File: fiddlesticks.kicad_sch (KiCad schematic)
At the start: 59 parts, among them J1 USB_C_Receptacle_USB2.0_16P, J2 Conn_01x04_Pin, J3 Conn_01x04_Pin, J4 Conn_02x04_Counter_Clockwise, J5 Conn_01x02_Pin, SW1 SW_Push, SW2 SW_Push, U1 STM32F411CEUx, U2 USBLC6-2SC6, U3 MCP1640Bx-xCHY, U4 SPX3819M5-L-3-3, Y1 8MHz 18pF

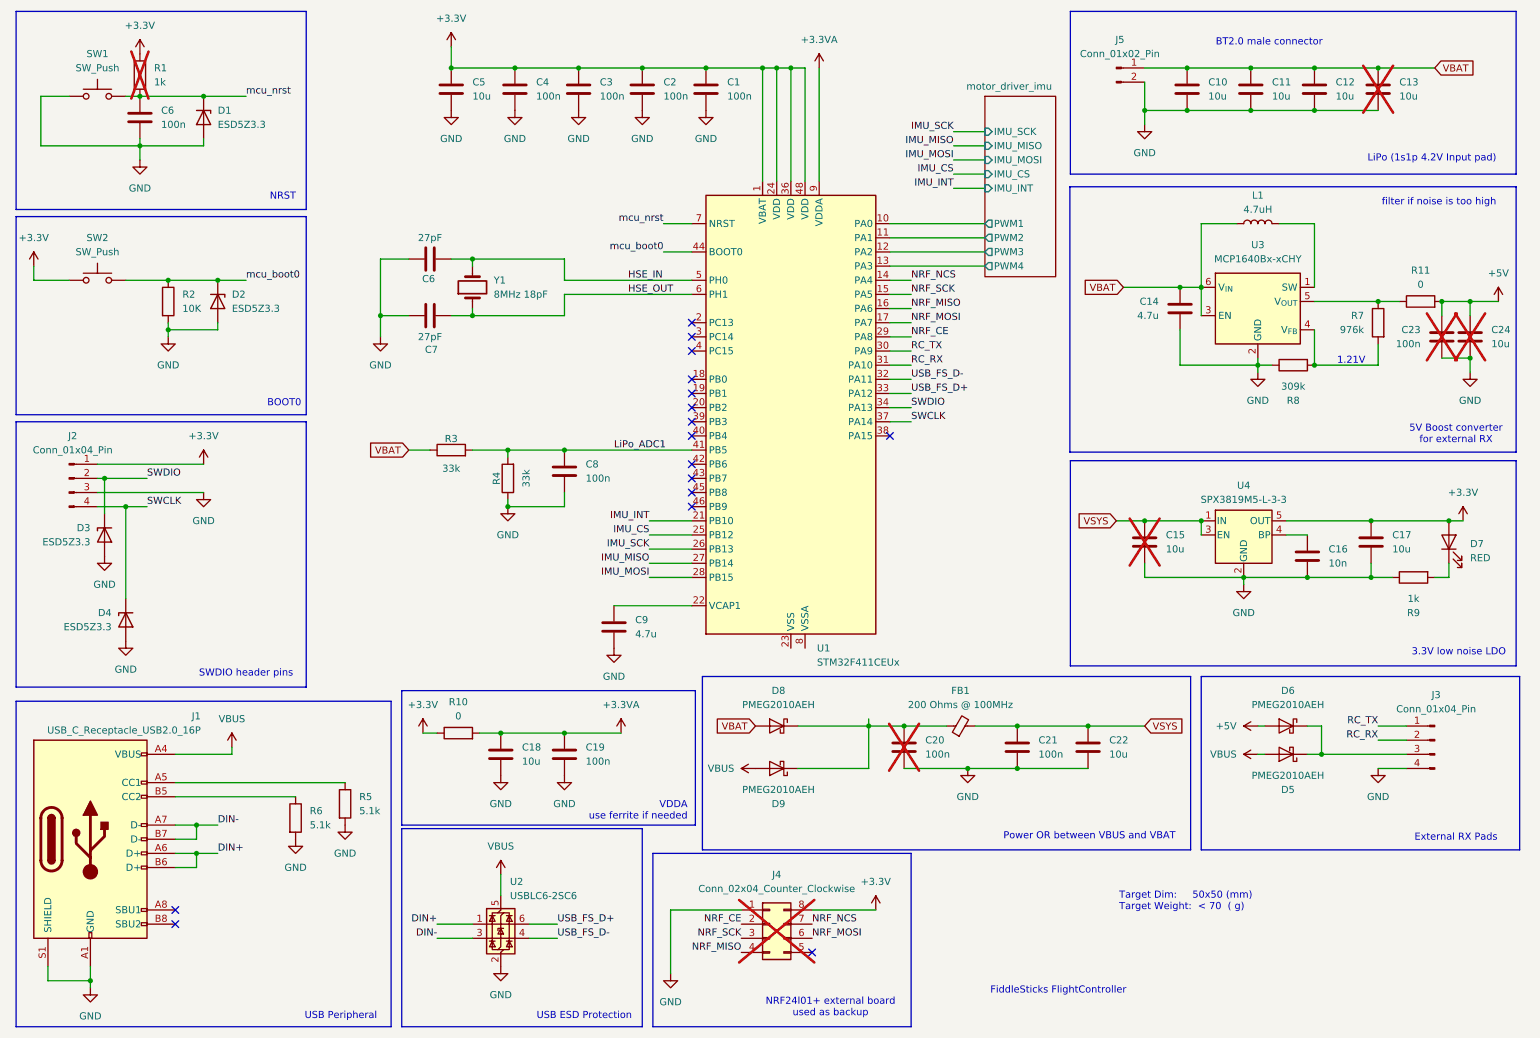
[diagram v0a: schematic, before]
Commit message: added 3.3 header for rx and changed flywheel diodes
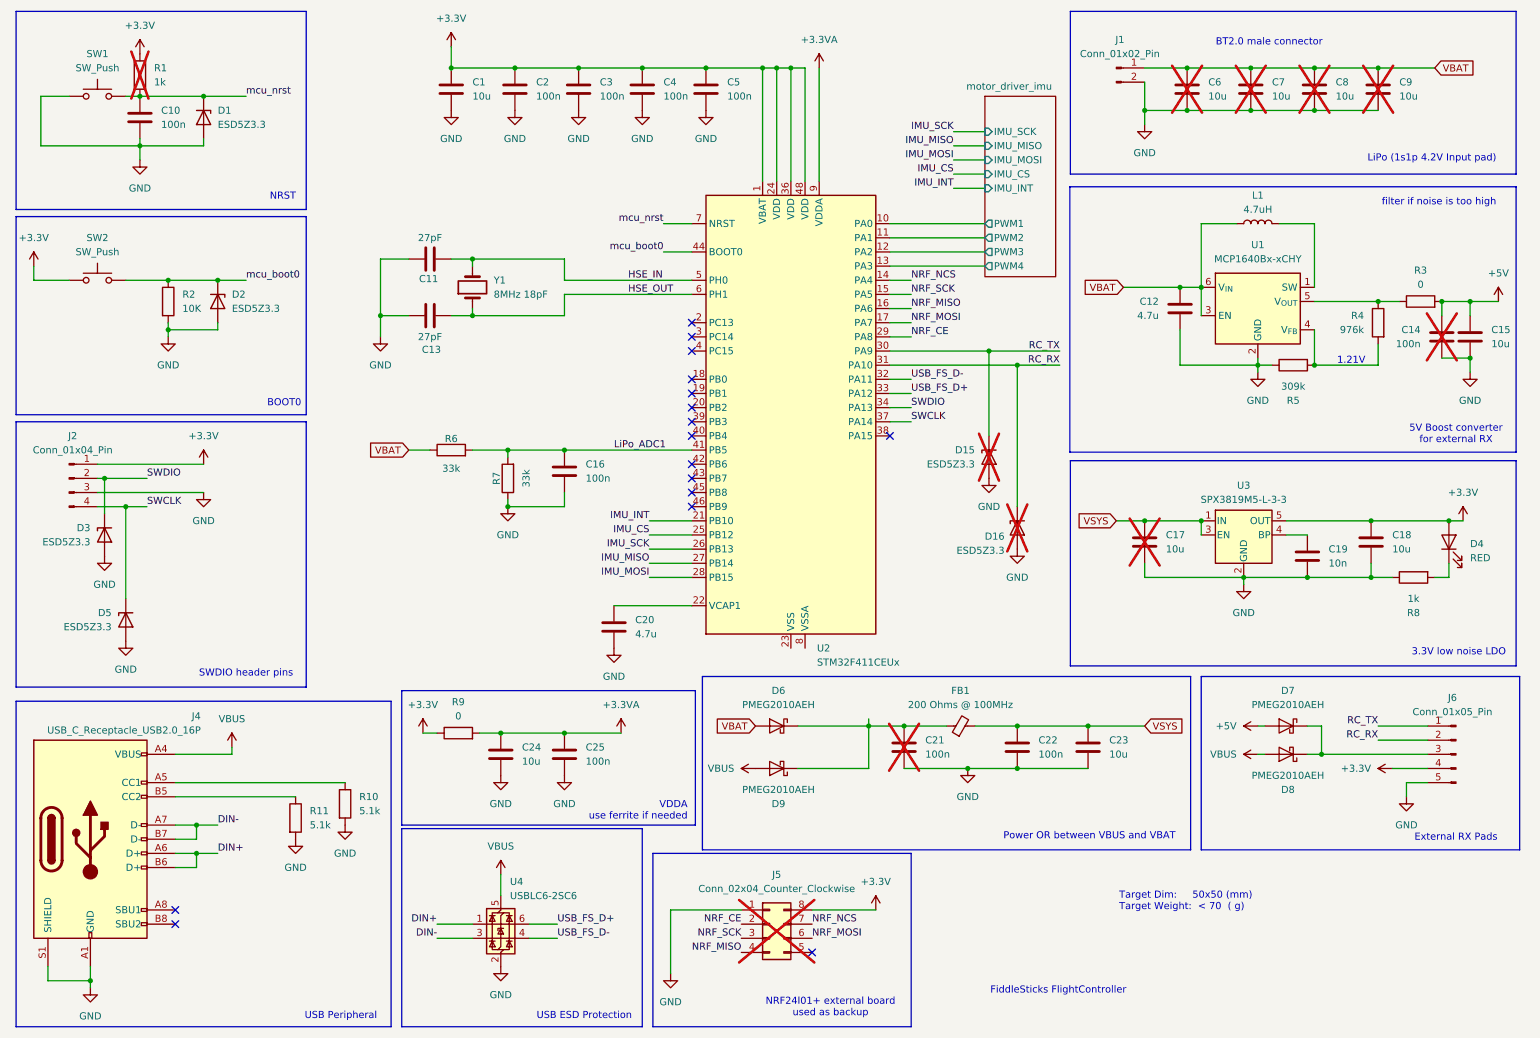
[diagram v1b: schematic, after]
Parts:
- removed J3: Conn_01x04_Pin, symbol Connector:Conn_01x04_Pin
- added D15, D16: ESD5Z3.3, Diode_SMD:D_SOD-523, symbol Diode:ESD5Zxx
- added J6: Conn_01x05_Pin, symbol Connector:Conn_01x05_Pin
- C15: renamed from C24; now fitted
- C6: renamed from C10; now not fitted
- C7: renamed from C11; now not fitted
- C8: renamed from C12; now not fitted
- renumbered C5 to C1, C6 to C10, C6 to C11, C14 to C12, C7 to C13, C23 to C14, C8 to C16, C15 to C17, C17 to C18, C16 to C19, C4 to C2, C9 to C20, C20 to C21, C21 to C22, C22 to C23, C18 to C24, C19 to C25, C2 to C4, C1 to C5, C13 to C9, D7 to D4, D4 to D5, D8 to D6, D6 to D7, D5 to D8, J5 to J1, J1 to J4, J4 to J5, R5 to R10, R6 to R11, R11 to R3, R7 to R4, R8 to R5, R3 to R6, R4 to R7, R9 to R8, R10 to R9, U3 to U1, U1 to U2, U4 to U3, U2 to U4
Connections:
- net +3.3V: now also J6.4 (Pin_4)
- net GND: now also D15.2 (A), D16.2 (A), J6.5 (Pin_5)
- net RC_RX: now also D16.1 (K), J6.2 (Pin_2)
- net RC_TX: now also D15.1 (K), J6.1 (Pin_1)
- net at D7.1 (K), D8.1 (K): now also J6.3 (Pin_3)

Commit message: updated footprints and changed crystal
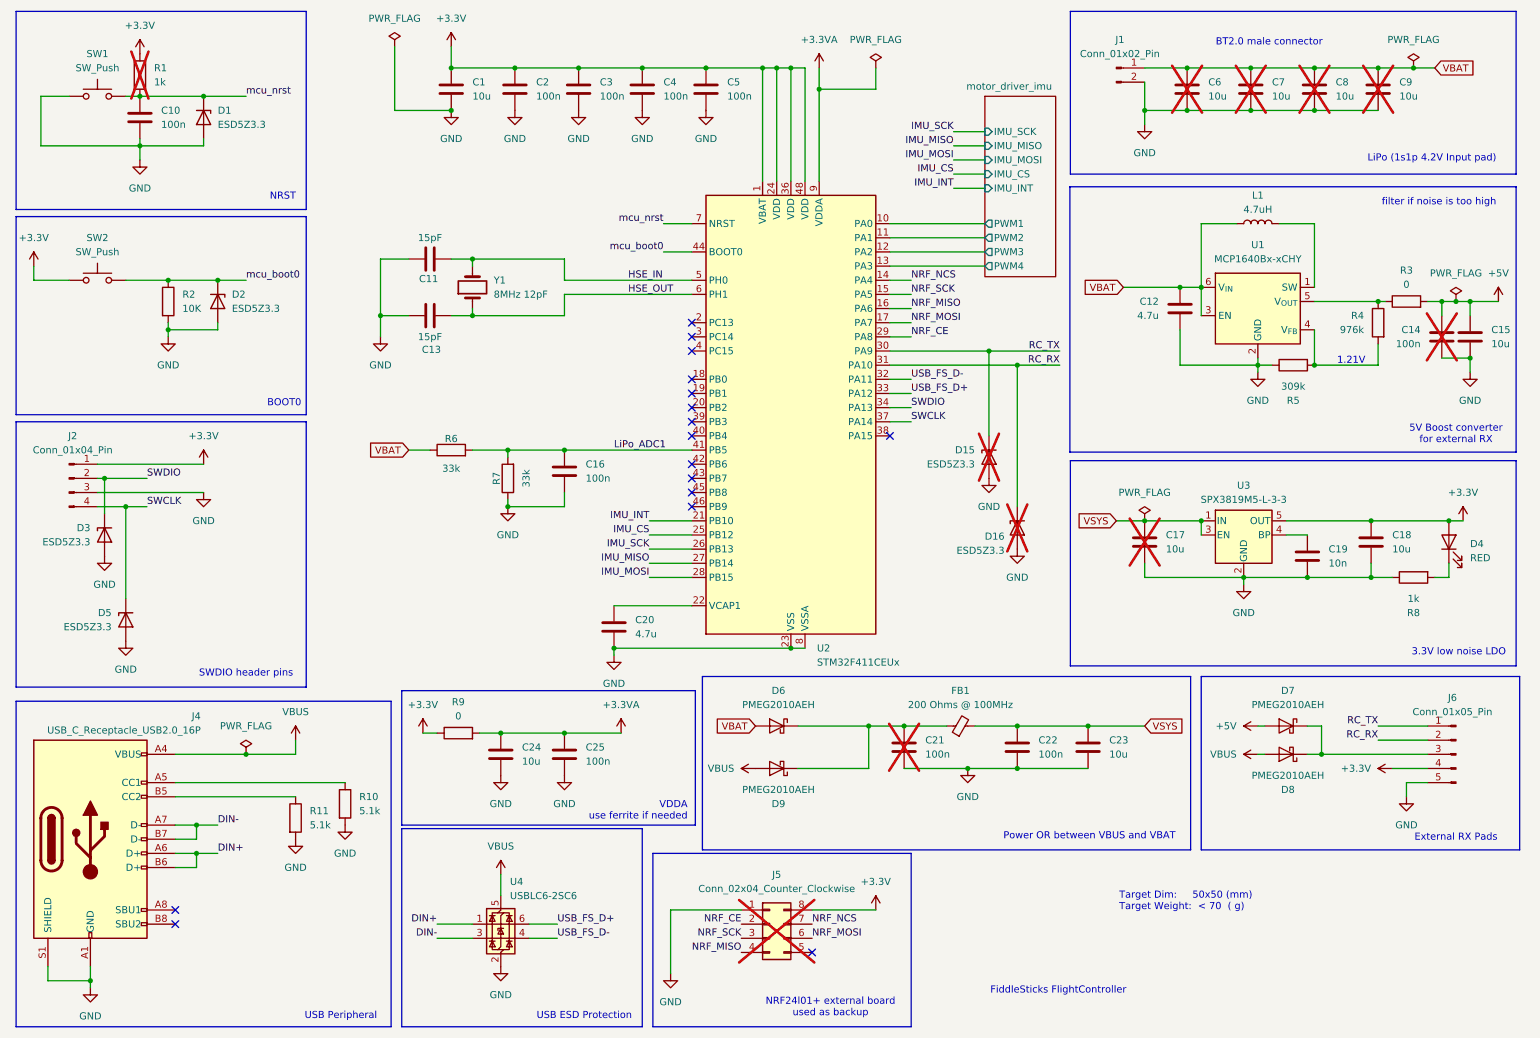
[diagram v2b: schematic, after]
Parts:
- C11, C13: value 27pF -> 15pF; footprint (none) -> Capacitor_SMD:C_0603_1608Metric_Pad1.08x0.95mm_HandSolder
- C12, C15, C17, C18, C20, C23, C24, C6, C7, C8, C9: footprint (none) -> Capacitor_SMD:C_0805_2012Metric_Pad1.18x1.45mm_HandSolder
- C14, C19, C21, C22, C25: footprint (none) -> Capacitor_SMD:C_0603_1608Metric_Pad1.08x0.95mm_HandSolder
- D4: footprint (none) -> LED_SMD:LED_0603_1608Metric_Pad1.05x0.95mm_HandSolder
- FB1, R1, R10, R11, R2, R3, R4, R5, R8, R9: footprint (none) -> Resistor_SMD:R_0603_1608Metric_Pad0.98x0.95mm_HandSolder
- J1: footprint (none) -> Connector_Wire:SolderWire-1sqmm_1x02_P5.4mm_D1.4mm_OD2.7mm
- J2: footprint (none) -> Connector_PinHeader_2.54mm:PinHeader_1x04_P2.54mm_Vertical
- J4: footprint (none) -> Connector_USB:USB_C_Receptacle_Palconn_UTC16-G
- J5: footprint (none) -> Connector_PinSocket_2.54mm:PinSocket_2x04_P2.54mm_Vertical
- J6: footprint (none) -> Connector_PinHeader_2.54mm:PinHeader_1x05_P2.54mm_Horizontal
- R6, R7: footprint Resistor_SMD:R_0805_2012Metric_Pad1.20x1.40mm_HandSolder -> Resistor_SMD:R_0603_1608Metric_Pad0.98x0.95mm_HandSolder
- Y1: value 8MHz 18pF -> 8MHz 12pF; footprint (none) -> Crystal:Crystal_SMD_5032-2Pin_5.0x3.2mm_HandSoldering
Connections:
- net GND: now also U2.23 (VSS), U2.35 (VSS), U2.47 (VSS), U2.49 (VSS), U2.8 (VSSA)
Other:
- moved on the sheet: R3

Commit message: added bulk cap near motors, started pcb layout routing
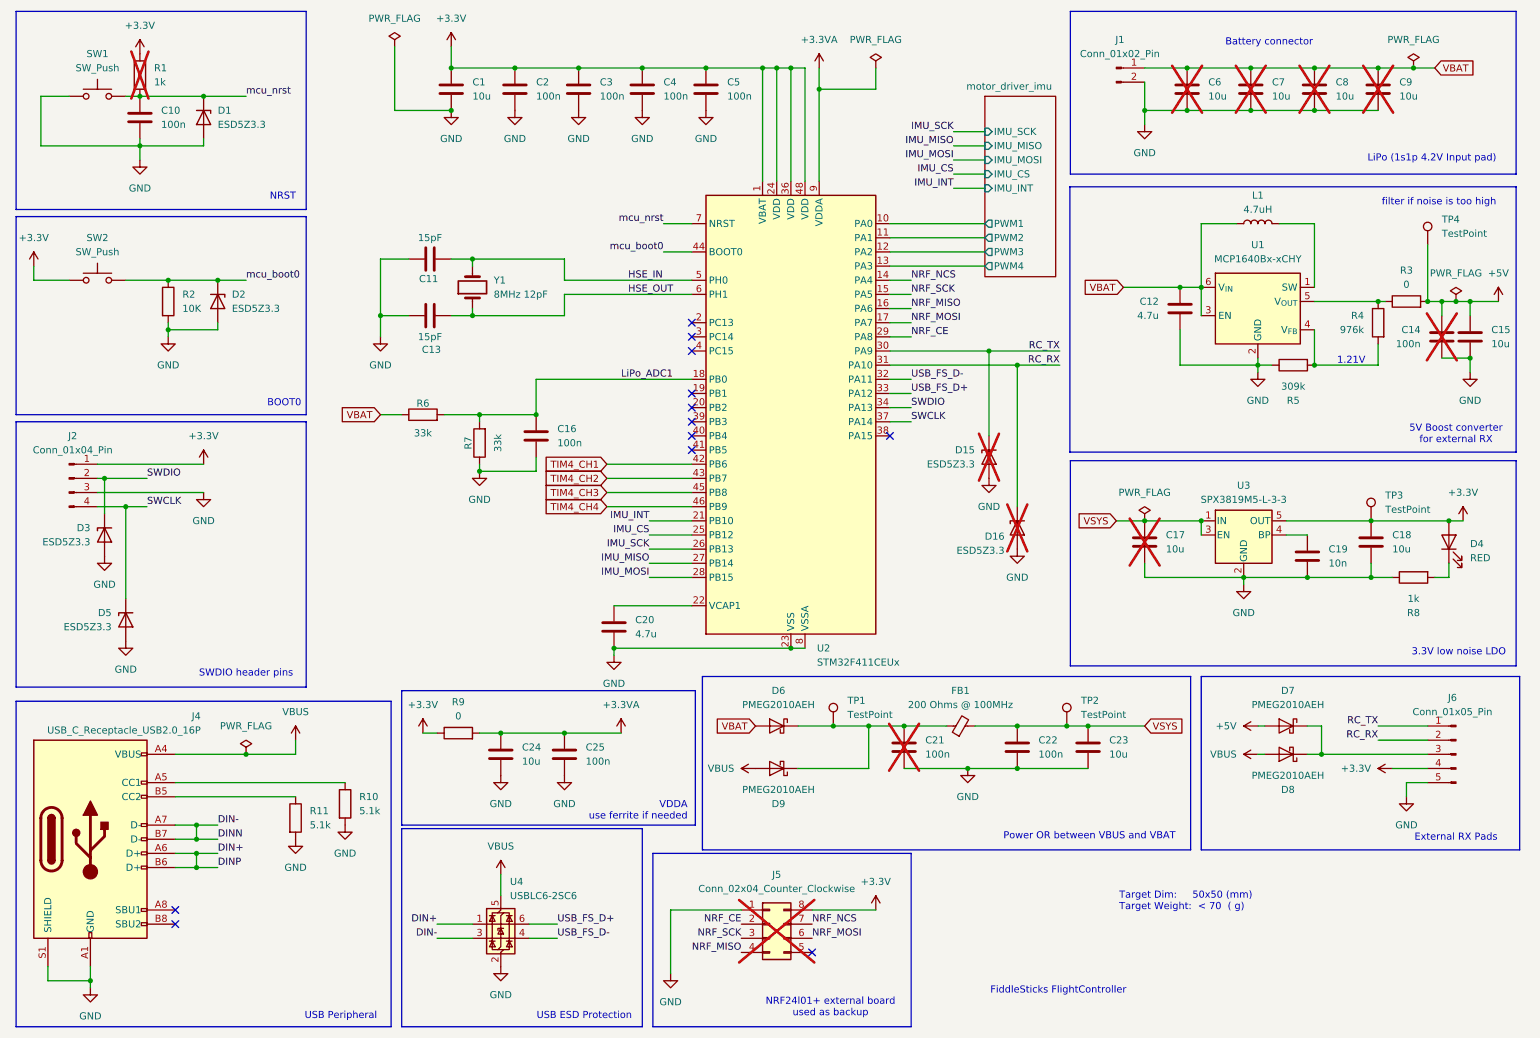
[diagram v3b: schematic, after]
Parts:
- added TP1, TP2, TP3, TP4: TestPoint, TestPoint:TestPoint_Pad_1.5x1.5mm, symbol Connector:TestPoint
- J4: MPN (none) -> TYPE-C-31-M-12
- L1: footprint (none) -> Inductor_SMD:L_0603_1608Metric_Pad1.05x0.95mm_HandSolder; MPN (none) -> LQM18PN4R7MFRL
- SW1, SW2: footprint (none) -> coolswitch:XUNPU TS-1088-AR02016; MPN (none) -> TS-1088-AR02016
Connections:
- net +3.3V: now also TP3.1
- net +5V: now also TP4.1
- net LiPo_ADC1: now also U2.18 (PB0); no longer U2.41 (PB5)
- net VSYS: now also TP2.1
- net at C21.1, D6.1 (K), D9.1 (K)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: now also TP1.1
- net TIM4_CH1: now reaches U2.42 (PB6)
- net TIM4_CH2: now reaches U2.43 (PB7)
- net TIM4_CH3: now reaches U2.45 (PB8)
- net TIM4_CH4: now reaches U2.46 (PB9)
- no-connect marks 16 -> 12
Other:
- note added: "Battery connector"
- note removed: "BT2.0 male connector"
- moved on the sheet: C16, R6, R7

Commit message: finished routing
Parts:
- removed C23, C6, C7, C8, C9: 10u, Capacitor_SMD:C_0805_2012Metric_Pad1.18x1.45mm_HandSolder, symbol Device:C
- removed J4: USB_C_Receptacle_USB2.0_16P, Connector_USB:USB_C_Receptacle_Palconn_UTC16-G, symbol Connector:USB_C_Receptacle_USB2.0_16P
- added J4: TYPE-C-31-M-12, USB_CUSTOM:HRO_TYPE-C-31-M-12, symbol USB_CUSTOM:TYPE-C-31-M-12
- added TP5, TP6, TP7: TestPoint, TestPoint:TestPoint_Pad_1.5x1.5mm, symbol Connector:TestPoint
- C21: value 100n -> 10uF; footprint Capacitor_SMD:C_0603_1608Metric_Pad1.08x0.95mm_HandSolder -> Capacitor_SMD:C_0805_2012Metric_Pad1.18x1.45mm_HandSolder
- C22: value 100n -> 100nF
- J5: now left out of the parts list
- R1: now fitted
- SW1, SW2: footprint coolswitch:XUNPU TS-1088-AR02016 -> coolswitch:SW_TS-1088-AR02016
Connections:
- net DIN+: now also J4.A6 (DP1), J4.B6 (DP2)
- net DIN-: now also J4.A7 (DN1), J4.B7 (DN2)
- net GND: now also J4.A1_B12 (GND), J4.B1_A12 (GND), J4.S1 (SHIELD), J4.S2 (SHIELD), J4.S3 (SHIELD), J4.S4 (SHIELD), TP5.1, TP6.1
- net VBUS: now also J4.A4_B9 (VBUS), J4.B4_A9 (VBUS), TP7.1
- net at R11.1: now also J4.B5 (CC2)
- net at R10.1: now also J4.A5 (CC1)
- net TIM4_CH1: no longer names the net of U2.42 (PB6)
- net TIM4_CH2: no longer names the net of U2.43 (PB7)
- net TIM4_CH3: no longer names the net of U2.45 (PB8)
- net TIM4_CH4: no longer names the net of U2.46 (PB9)
- no-connect marks 12 -> 21
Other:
- moved on the sheet: R10, R11

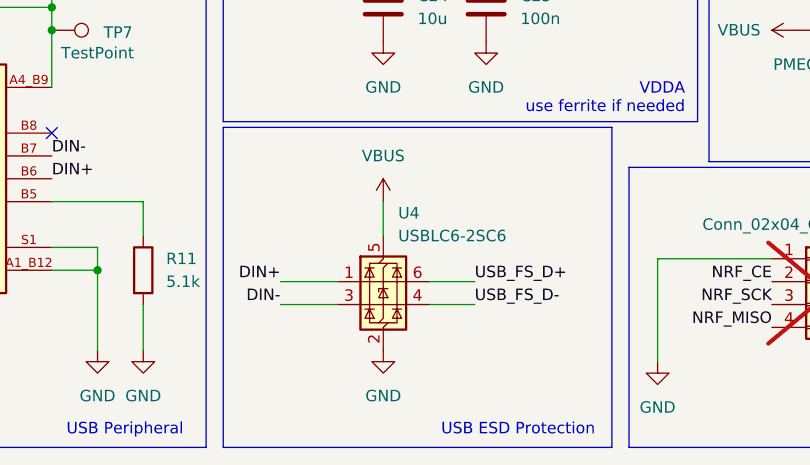
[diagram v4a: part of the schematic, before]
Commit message: fixed usb routing, and esd/pull ups/pull downs placement
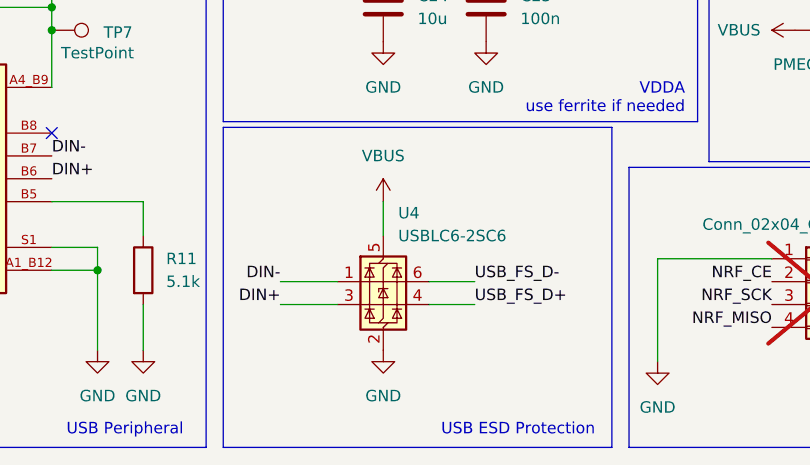
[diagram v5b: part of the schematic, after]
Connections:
- net DIN+: now also U4.3 (I/O2); no longer U4.1 (I/O1)
- net DIN-: now also U4.1 (I/O1); no longer U4.3 (I/O2)
- net USB_FS_D+: now also U4.4 (I/O2); no longer U4.6 (I/O1)
- net USB_FS_D-: now also U4.6 (I/O1); no longer U4.4 (I/O2)
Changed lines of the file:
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@@
 	)
 	(label "DIN+"
-		(at 88.9 177.8 180)
+		(at 88.9 180.34 180)
 		(effects
 			(font
@@
 	)
 	(label "USB_FS_D+"
-		(at 110.49 177.8 0)
+		(at 110.49 180.34 0)
 		(effects
 			(font
@@
 	)
 	(label "USB_FS_D-"
-		(at 110.49 180.34 0)
+		(at 110.49 177.8 0)
 		(effects
 			(font
@@
 	)
 	(label "DIN-"
-		(at 88.9 180.34 180)
+		(at 88.9 177.8 180)
 		(effects
 			(font
